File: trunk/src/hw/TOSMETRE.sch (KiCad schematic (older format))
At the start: 12 parts, among them J1 Conn_01x01_Female, J2 Conn_01x01_Female, J3 Conn_01x01, J4 Conn_01x01, J5 Conn_01x03, U1 16F88_SSOP, U2 L7805

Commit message: 
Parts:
- C1, C2: symbol C -> Device:C
- C5: symbol CP_Small -> Device:CP_Small
- D1: symbol D -> Device:D
- DS1: symbol WC1602A -> TOSMETRE-rescue:WC1602A
- J1, J2: symbol Conn_01x01_Female -> TOSMETRE-rescue:Conn_01x01_Female
- J3, J4: symbol Conn_01x01 -> TOSMETRE-rescue:Conn_01x01
- J5: symbol Conn_01x05 -> TOSMETRE-rescue:Conn_01x05
- U1: symbol 16F88_SSOP -> 16F88:16F88_SSOP
- U2: symbol L7805 -> TOSMETRE-rescue:L7805
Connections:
- wire segments 50 -> 57
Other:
- moved on the sheet: C5
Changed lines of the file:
@@
-EESchema Schematic File Version 2
-LIBS:TOSMETRE-rescue
-LIBS:power
-LIBS:device
-LIBS:switches
-LIBS:relays
-LIBS:motors
-LIBS:transistors
-LIBS:conn
-LIBS:linear
-LIBS:regul
-LIBS:74xx
-LIBS:cmos4000
-LIBS:adc-dac
-LIBS:memory
-LIBS:xilinx
-LIBS:microcontrollers
-LIBS:dsp
-LIBS:microchip
-LIBS:analog_switches
-LIBS:motorola
-LIBS:texas
-LIBS:intel
-LIBS:audio
-LIBS:interface
-LIBS:digital-audio
-LIBS:philips
-LIBS:display
-LIBS:cypress
-LIBS:siliconi
-LIBS:opto
-LIBS:atmel
-LIBS:contrib
-LIBS:valves
-LIBS:16F88
+EESchema Schematic File Version 4
 LIBS:TOSMETRE-cache
-EELAYER 25 0
+EELAYER 29 0
 EELAYER END
 $Descr A4 11693 8268
@@
 $EndDescr
 $Comp
-L D D1
+L Device:D D1
 U 1 1 5A324E39
 P 3950 2000
@@
 $EndComp
 $Comp
-L L7805 U2
+L TOSMETRE-rescue:L7805 U2
 U 1 1 5A33E692
 P 5350 2000
@@
 $EndComp
 $Comp
-L GNDREF #PWR01
+L power:GNDREF #PWR01
 U 1 1 5A343ADA
-P 6200 3150
-F 0 "#PWR01" H 6200 2900 50  0001 C CNN
-F 1 "GNDREF" H 6200 3000 50  0000 C CNN
-F 2 "" H 6200 3150 50  0001 C CNN
-F 3 "" H 6200 3150 50  0001 C CNN
-	1    6200 3150
-	0    1    1    0
-$EndComp
-$Comp
-L GNDREF #PWR02
+P 7200 3150
+F 0 "#PWR01" H 7200 2900 50  0001 C CNN
+F 1 "GNDREF" H 7200 3000 50  0000 C CNN
+F 2 "" H 7200 3150 50  0001 C CNN
+F 3 "" H 7200 3150 50  0001 C CNN
+	1    7200 3150
+	0    -1   1    0
+$EndComp
+$Comp
+L power:GNDREF #PWR02
 U 1 1 5A343C5D
 P 10550 2000
@@
 $EndComp
 $Comp
-L C C1
+L Device:C C1
 U 1 1 5A3C3936
 P 4500 2250
@@
 $EndComp
 $Comp
-L GNDREF #PWR03
+L power:GNDREF #PWR03
 U 1 1 5A3C3EAC
 P 6600 6050
@@
 $EndComp
 $Comp
-L GNDREF #PWR04
+L power:GNDREF #PWR04
 U 1 1 5AA42E24
 P 5350 2500
@@
 $EndComp
 $Comp
-L GNDREF #PWR05
+L power:GNDREF #PWR05
 U 1 1 5AA44D09
 P 4500 2500
@@
 $EndComp
 $Comp
-L GNDREF #PWR06
+L power:GNDREF #PWR06
 U 1 1 5AA44E43
 P 4500 2500
@@
 $EndComp
 $Comp
-L CP_Small C5
+L Device:CP_Small C5
 U 1 1 5AA53058
-P 6400 3150
-F 0 "C5" H 6410 3220 50  0000 L CNN
-F 1 "CP_Small" H 6410 3070 50  0000 L CNN
-F 2 "Capacitors_SMD:CP_Elec_3x5.3" H 6400 3150 50  0001 C CNN
-F 3 "" H 6400 3150 50  0001 C CNN
-	1    6400 3150
-	0    1    1    0
-$EndComp
-$Comp
-L 16F88_SSOP U1
+P 7000 3150
+F 0 "C5" H 7010 3220 50  0000 L CNN
+F 1 "CP_Small" H 7010 3070 50  0000 L CNN
+F 2 "Capacitors_SMD:CP_Elec_3x5.3" H 7000 3150 50  0001 C CNN
+F 3 "" H 7000 3150 50  0001 C CNN
+	1    7000 3150
+	0    -1   1    0
+$EndComp
+$Comp
+L 16F88:16F88_SSOP U1
 U 1 1 5AA53019
 P 6600 4900
@@
 REF
 $Comp
-L WC1602A DS1
+L TOSMETRE-rescue:WC1602A DS1
 U 1 1 5A3242FC
 P 9500 2000
@@
 $EndComp
 $Comp
-L GNDREF #PWR07
+L power:GNDREF #PWR07
 U 1 1 5AA93D0C
 P 3300 2500
@@
 $EndComp
 $Comp
-L GNDREF #PWR08
+L power:GNDREF #PWR08
 U 1 1 5AA93D13
 P 3300 2500
@@
 $EndComp
 $Comp
-L Conn_01x01_Female J1
+L TOSMETRE-rescue:Conn_01x01_Female J1
 U 1 1 5AA94180
 P 2950 2000
@@
 $EndComp
 $Comp
-L Conn_01x01_Female J2
+L TOSMETRE-rescue:Conn_01x01_Female J2
 U 1 1 5AA941DB
 P 2950 2350
@@
 $EndComp
 $Comp
-L C C2
+L Device:C C2
 U 1 1 5AACE979
 P 6050 2250
@@
 $EndComp
 $Comp
-L GNDREF #PWR09
+L power:GNDREF #PWR09
 U 1 1 5AAD17B7
 P 6050 2500
@@
 $EndComp
 $Comp
-L Conn_01x01 J4
+L TOSMETRE-rescue:Conn_01x01 J4
 U 1 1 5AB12A8D
 P 4950 3950
@@
 $EndComp
 $Comp
-L Conn_01x01 J3
+L TOSMETRE-rescue:Conn_01x01 J3
 U 1 1 5AB12B4B
 P 4950 3650
@@
 $EndComp
 $Comp
-L Conn_01x05 J5
+L TOSMETRE-rescue:Conn_01x05 J5
 U 1 1 5B140FD8
 P 8400 4800
@@
 $EndComp
 $Comp
-L GNDREF #PWR010
+L power:GNDREF #PWR010
 U 1 1 5B1453B6
 P 8000 5650
@@
 $EndComp
 Wire Wire Line
-	6600 5400 6600 6050
+	6600 5400 6600 6000
 Connection ~ 6600 2000
 Wire Wire Line
@@
 	10550 2000 10300 2000
 Wire Wire Line
-	4100 2000 5050 2000
+	4100 2000 4500 2000
 Wire Wire Line
 	5350 2300 5350 2500
@@
 	7000 4200 9900 4200
 Wire Wire Line
-	6800 4000 10100 4000
+	6800 4000 7500 4000
 Wire Wire Line
 	7000 5400 7000 6000
@@
 	6050 2400 6050 2500
 Wire Wire Line
-	6500 3150 6700 3150
-Wire Wire Line
-	6300 3150 6200 3150
+	6900 3150 6700 3150
+Wire Wire Line
+	7100 3150 7200 3150
 Wire Wire Line
 	8000 5000 8000 5650
@@
 	7100 5400 7100 5900
 Wire Wire Line
-	7100 5900 8900 5900
+	7100 5900 7500 5900
 Wire Wire Line
 	8200 4900 7500 4900
@@
 	6900 4100 6900 4400
 Wire Wire Line
-	10000 4100 6900 4100
+	10000 4100 8000 4100
 Wire Wire Line
 	8200 4700 8000 4700
@@
 Connection ~ 6050 2000
 Wire Wire Line
-	5650 2000 8700 2000
+	5650 2000 6050 2000
+Wire Wire Line
+	6600 2000 8700 2000
+Wire Wire Line
+	4500 2000 5050 2000
+Wire Wire Line
+	6600 6000 6600 6050
+Wire Wire Line
+	7500 4000 10100 4000
+Wire Wire Line
+	7500 5900 8900 5900
+Wire Wire Line
+	8000 4100 6900 4100
+Wire Wire Line
+	6050 2000 6600 2000
 $EndSCHEMATC

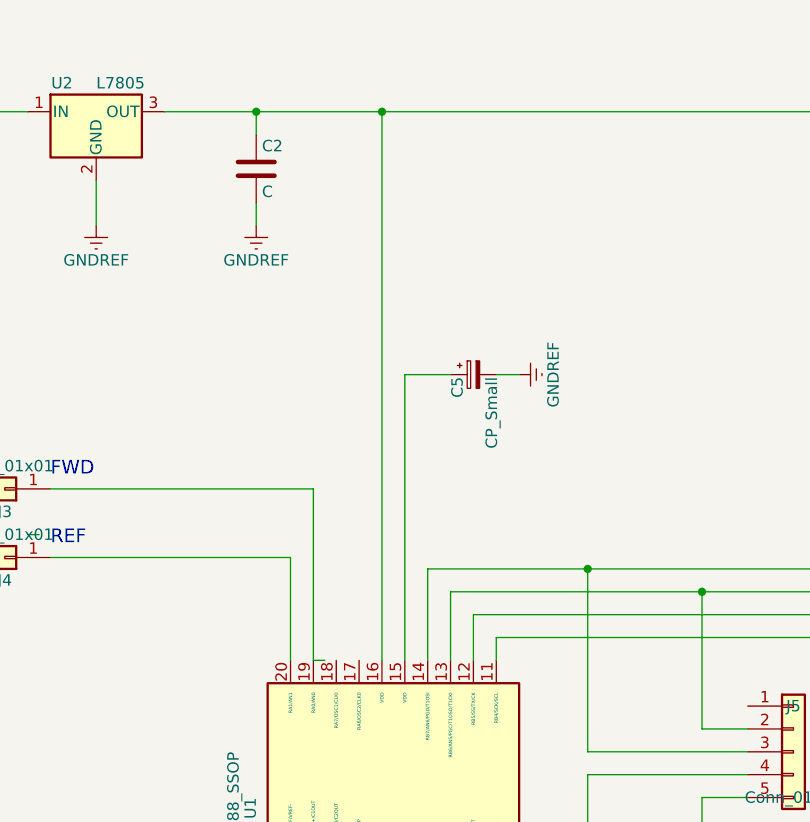
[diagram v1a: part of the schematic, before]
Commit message: oubli de jonction apres re re re verif et re re re modif
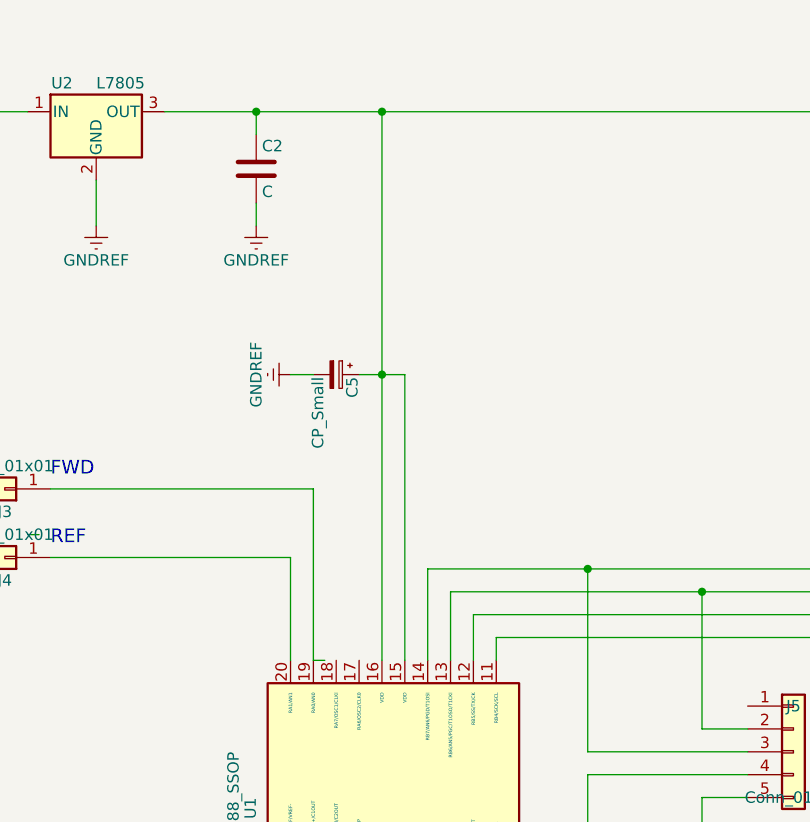
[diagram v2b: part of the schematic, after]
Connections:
- wire segments 57 -> 59
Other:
- moved on the sheet: C5
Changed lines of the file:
@@
 L power:GNDREF #PWR01
 U 1 1 5A343ADA
-P 7200 3150
-F 0 "#PWR01" H 7200 2900 50  0001 C CNN
-F 1 "GNDREF" H 7200 3000 50  0000 C CNN
-F 2 "" H 7200 3150 50  0001 C CNN
-F 3 "" H 7200 3150 50  0001 C CNN
-	1    7200 3150
-	0    -1   1    0
+P 6200 3150
+F 0 "#PWR01" H 6200 2900 50  0001 C CNN
+F 1 "GNDREF" H 6200 3000 50  0000 C CNN
+F 2 "" H 6200 3150 50  0001 C CNN
+F 3 "" H 6200 3150 50  0001 C CNN
+	1    6200 3150
+	0    1    1    0
 $EndComp
 $Comp
@@
 L Device:CP_Small C5
 U 1 1 5AA53058
-P 7000 3150
-F 0 "C5" H 7010 3220 50  0000 L CNN
-F 1 "CP_Small" H 7010 3070 50  0000 L CNN
-F 2 "Capacitors_SMD:CP_Elec_3x5.3" H 7000 3150 50  0001 C CNN
-F 3 "" H 7000 3150 50  0001 C CNN
-	1    7000 3150
-	0    -1   1    0
+P 6400 3150
+F 0 "C5" H 6410 3220 50  0000 L CNN
+F 1 "CP_Small" H 6410 3070 50  0000 L CNN
+F 2 "Capacitors_SMD:CP_Elec_3x5.3" H 6400 3150 50  0001 C CNN
+F 3 "" H 6400 3150 50  0001 C CNN
+	1    6400 3150
+	0    1    1    0
 $EndComp
 $Comp
@@
 	4500 2500 4500 2400
 Wire Wire Line
-	6600 2000 6600 4400
+	6600 2000 6600 3150
 Wire Wire Line
 	7100 4300 9800 4300
@@
 	6050 2400 6050 2500
 Wire Wire Line
-	6900 3150 6700 3150
-Wire Wire Line
-	7100 3150 7200 3150
+	6500 3150 6600 3150
+Wire Wire Line
+	6300 3150 6200 3150
 Wire Wire Line
 	8000 5000 8000 5650
@@
 Wire Wire Line
 	6050 2000 6600 2000
+Connection ~ 6600 3150
+Wire Wire Line
+	6600 3150 6600 4400
+Wire Wire Line
+	6600 3150 6700 3150
 $EndSCHEMATC
